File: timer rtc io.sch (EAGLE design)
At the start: 78 parts, among them T1 BC547, U1 74HC245, U10 74HC688, U11 74LS30N, U12 74LS00N, U13 74HC32, U14 74HC04, U15 74HC08, U16 74HC688, U17 74HC138, U18 74HC138, U19 74HC573, U2 74HC245, U20 74HC573, U21 74HC573, U22 74HC573, U23 74HC573, U24 NE555, U3 74HC245, U4 74HC688, U6 74HC74, U7 74HC590, U8 74HC688, U9 BQ4845, X1 32.768KHz, Y1 4.096MHz

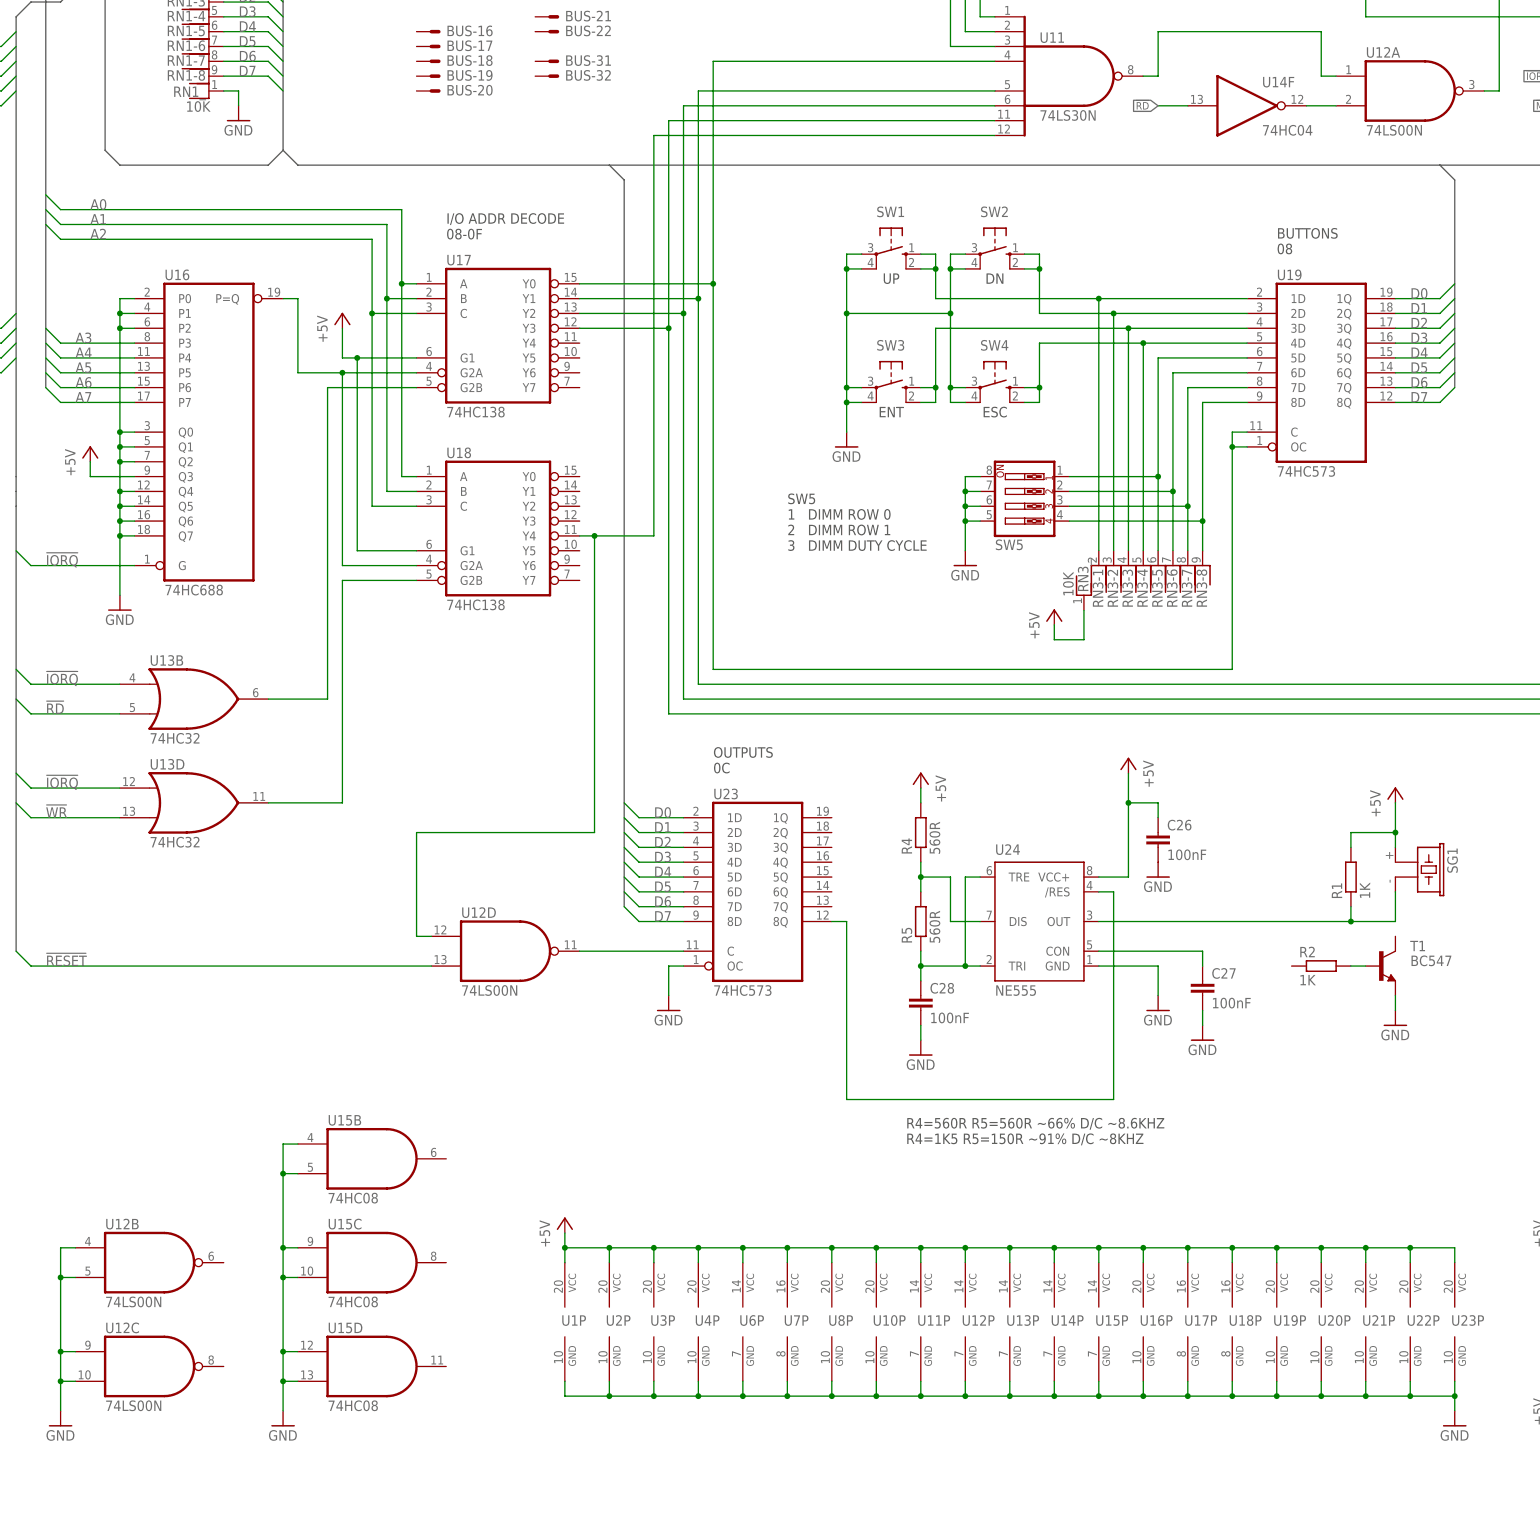
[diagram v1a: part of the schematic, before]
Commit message: Update values for U11 and U12
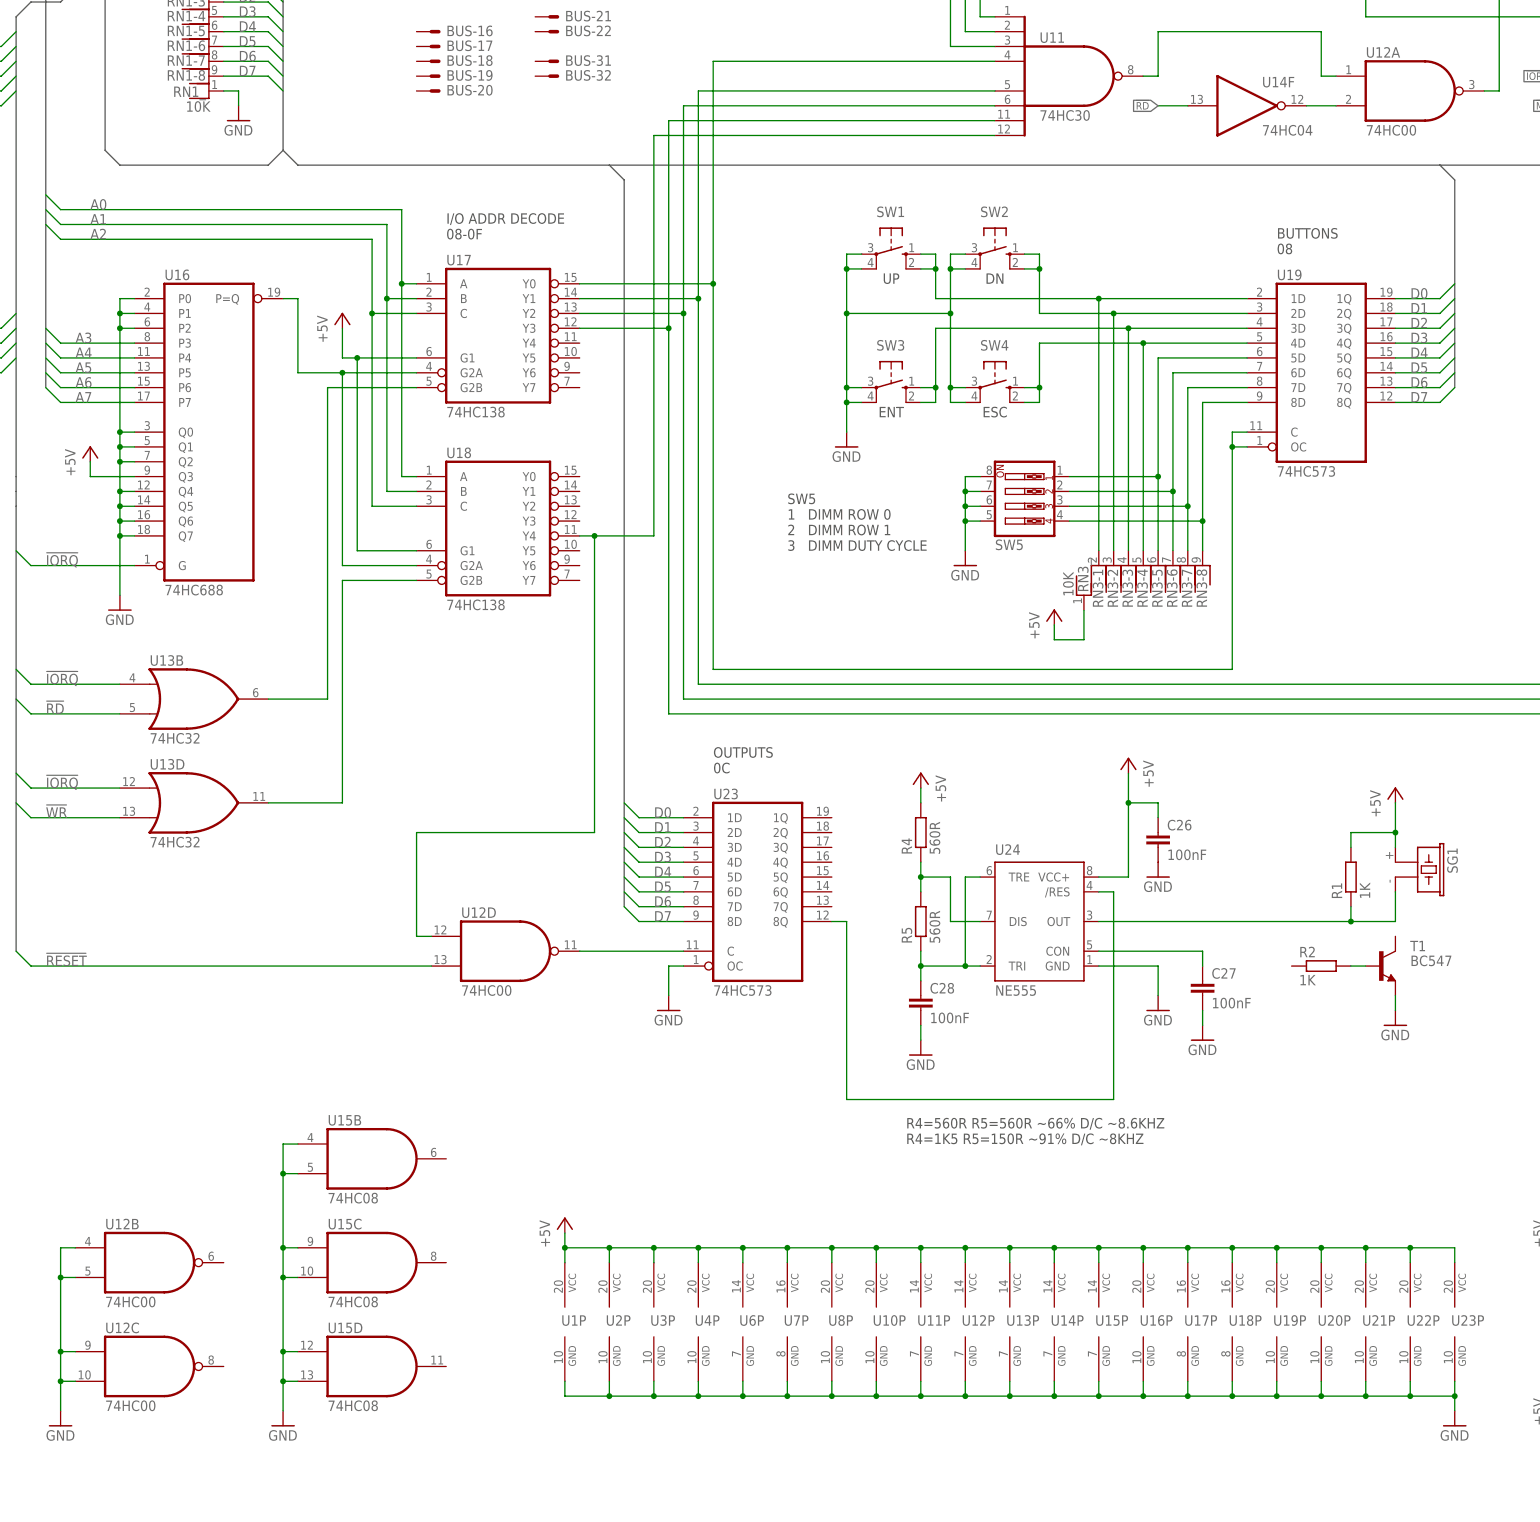
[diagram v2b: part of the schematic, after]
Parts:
- U11: value 74LS30N -> 74HC30
- U12: value 74LS00N -> 74HC00
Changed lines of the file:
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@@
 <part name="T1" library="transistor" deviceset="BC547" device=""/>
 <part name="R2" library="rcl" deviceset="R-EU_" device="0207/10" value="1K"/>
-<part name="U11" library="74xx-us" deviceset="74*30" device="N" technology="LS"/>
-<part name="U12" library="74xx-us" deviceset="74*00" device="N" technology="LS"/>
+<part name="U11" library="74xx-us" deviceset="74*30" device="N" technology="LS" value="74HC30"/>
+<part name="U12" library="74xx-us" deviceset="74*00" device="N" technology="LS" value="74HC00"/>
 <part name="GND23" library="supply1" deviceset="GND" device=""/>
 <part name="GND24" library="supply1" deviceset="GND" device=""/>
